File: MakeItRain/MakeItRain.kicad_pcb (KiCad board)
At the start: 4 copper layers, 151.1 x 71.1 mm, 80 parts, among them IC3 OPA2340PA, IC4 LTV-846S, J1 Conn_02x15_Odd_Even, J2 Conn_02x19_Odd_Even, J3 Conn_01x19, J4 Conn_01x01, J5 Conn_01x04, P1 Screw_Terminal_01x02, Q1 2N7000, Q10 2N7000, Q11 2N7000, Q12 IRF9Z34NPBF, Q13 IRF9Z34NPBF, Q2 2N7000, Q3 IRF9Z34NPBF, Q4 2N7000, Q5 2N7000, Q6 IRF9Z34NPBF, Q7 2N7000, Q8 2N7000, Q9 IRF9Z34NPBF, U2 178.6165.0001

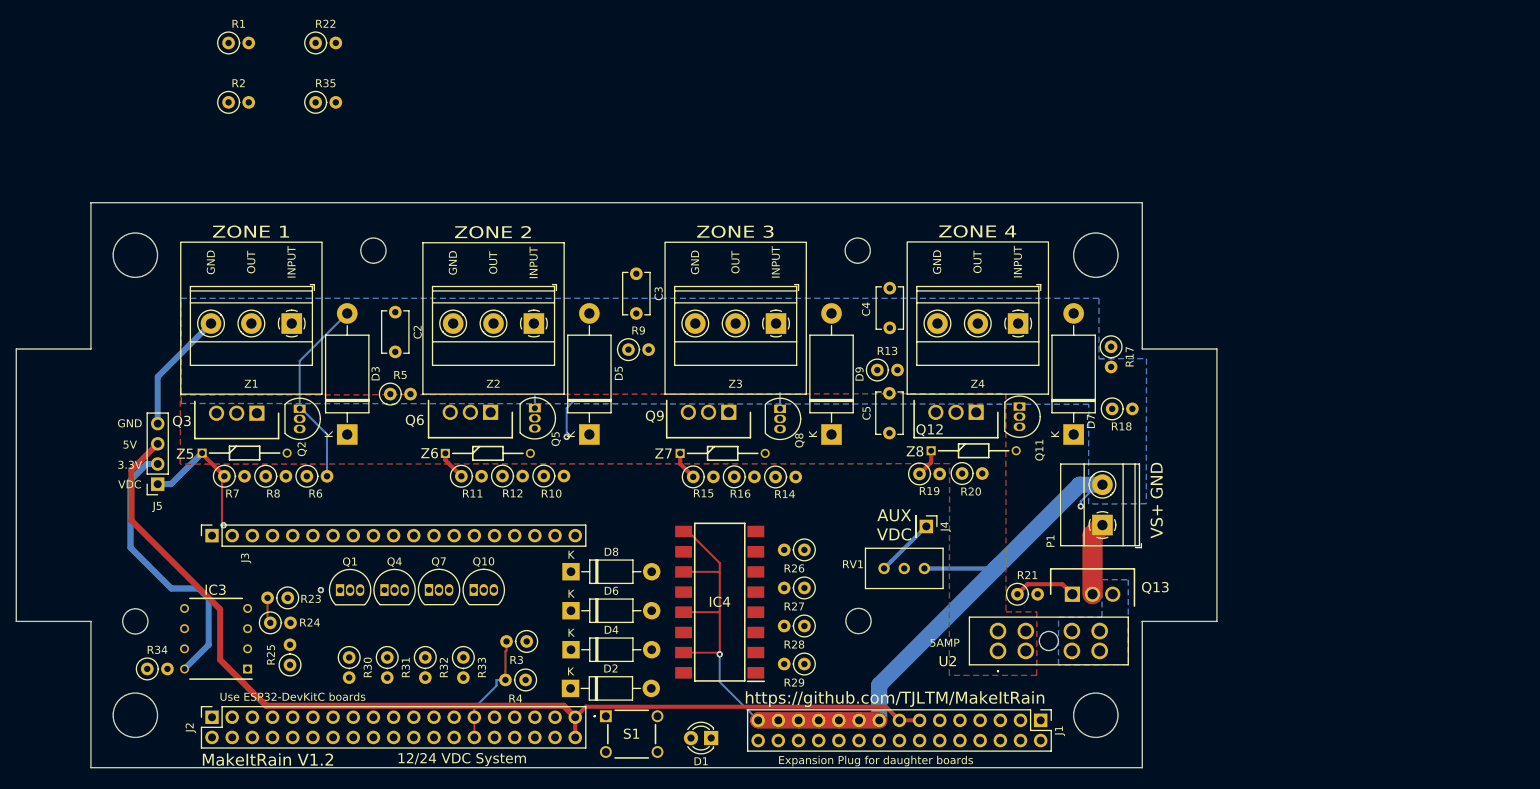
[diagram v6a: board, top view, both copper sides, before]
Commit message: working on getting the test code for the MCP23008 into the fw. working on the pins and getting all of that stuff placed on the PCB.
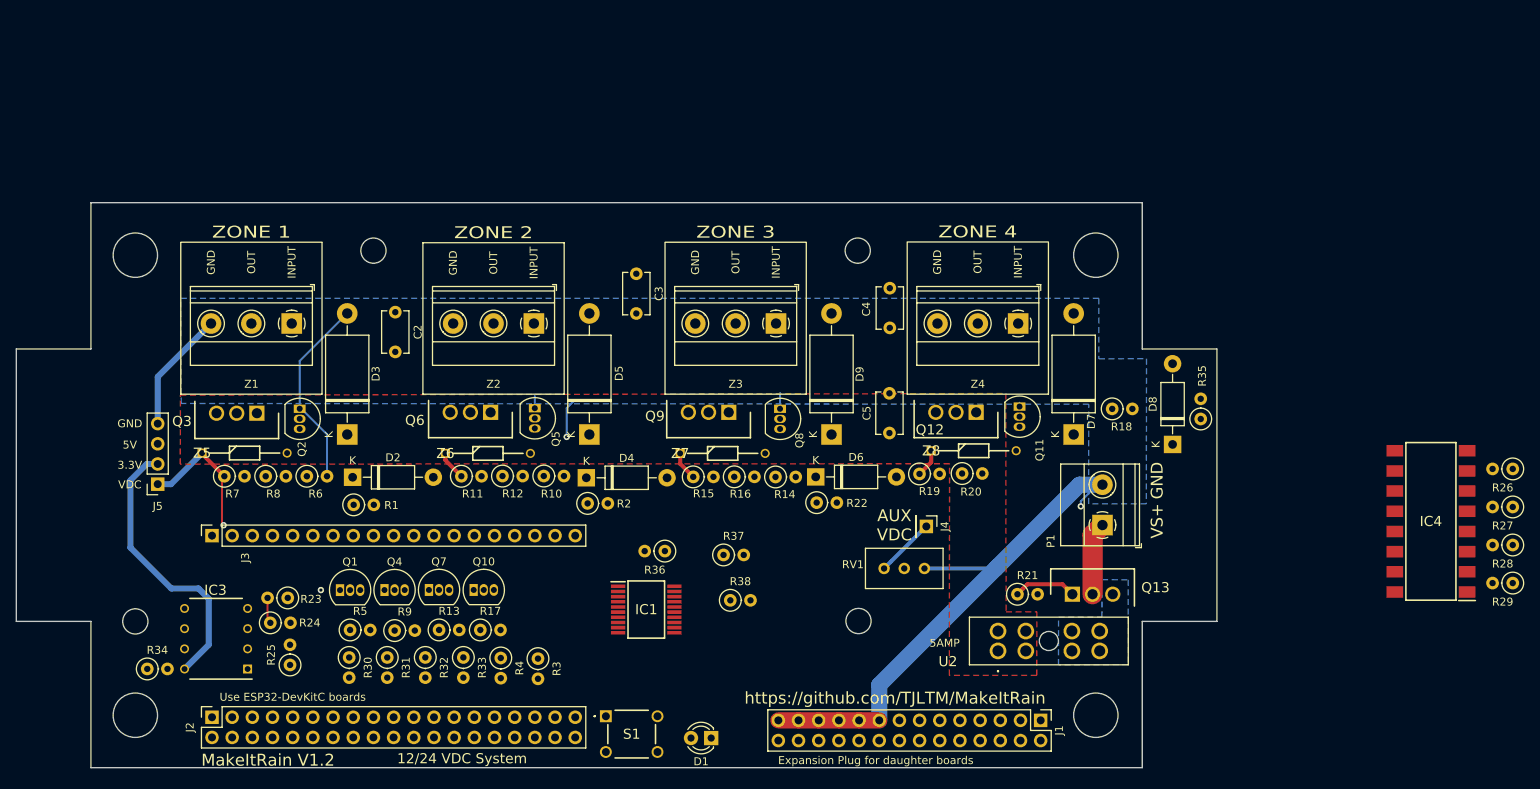
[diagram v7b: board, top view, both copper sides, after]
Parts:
- added IC1: MCP23008T-E_SS, SamacSys_Parts:SOP65P780X200-20N, F.Cu at (120.7, 107.1)
- added R36: 10k, Resistor_THT:R_Axial_DIN0207_L6.3mm_D2.5mm_P2.54mm_Vertical, F.Cu at (123.0, 99.7)
- added R37: 10k, Resistor_THT:R_Axial_DIN0207_L6.3mm_D2.5mm_P2.54mm_Vertical, F.Cu at (130.4, 100.2)
- added R38: 10k, Resistor_THT:R_Axial_DIN0207_L6.3mm_D2.5mm_P2.54mm_Vertical, F.Cu at (131.3, 105.9)
- J1: value Conn_02x15_Odd_Even -> Conn_02x14_Odd_Even; footprint Connector_PinHeader_2.54mm:PinHeader_2x15_P2.54mm_Vertical -> Connector_PinHeader_2.54mm:PinHeader_2x14_P2.54mm_Vertical
- moved R35 118.3 mm to (190.5, 83.1), turned to 90 degrees
- moved IC4 90.1 mm to (219.5, 96.0)
- moved R26 89.7 mm to (229.8, 89.4)
- moved R27 89.7 mm to (229.8, 94.2)
- moved R28 89.7 mm to (229.8, 99.0)
- moved R29 89.7 mm to (229.8, 103.8)
- moved R17 87.0 mm to (99.8, 109.7), turned to 0 degrees
- moved R22 85.6 mm to (142.2, 93.6)
- moved D8 77.4 mm to (187.0, 86.3), turned to 90 degrees
- moved R2 67.8 mm to (113.3, 93.7)
- moved R13 64.1 mm to (94.6, 109.7)
- moved R1 60.2 mm to (83.9, 93.9)
- moved R9 46.0 mm to (89.0, 109.7)
- moved D2 38.2 mm to (83.7, 90.4)
- moved D6 35.1 mm to (142.0, 90.4)
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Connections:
- net /Zone1IO/ZoneOutputTTL renamed Z1
- net /Zone2IO/ZoneOutputTTL renamed Z2
- net /Zone3IO/ZoneOutputTTL renamed Z3
- net /Zone4IO/ZoneOutputTTL renamed Z4
- IC3 pad 1: D36 -> D25
- IC3 pad 2: D36 -> D25
- J1 pad 10: unconnected-(J1-Pad10) -> Z6
- J1 pad 12: unconnected-(J1-Pad12) -> Z5
- J1 pad 13: +5V -> +3V3
- J1 pad 14: unconnected-(J1-Pad14) -> D26
- J1 pad 16: unconnected-(J1-Pad16) -> D23
- J1 pad 17: GND -> +5V
- J1 pad 18: unconnected-(J1-Pad18) -> D19
- J1 pad 19: GND -> +5V
- J1 pad 20: unconnected-(J1-Pad20) -> D18
- J1 pad 22: unconnected-(J1-Pad22) -> D17
- J1 pad 24: unconnected-(J1-Pad24) -> D16
- J1 pad 26: unconnected-(J1-Pad26) -> TX
- J1 pad 28: TX -> RX
- J1 pad 6: unconnected-(J1-Pad6) -> Z8
- J1 pad 8: unconnected-(J1-Pad8) -> Z7
- J1 pad 9: +VDC -> +3V3
- J2 pad 35: unconnected-(J2-Pad35) -> GND
- R25 pad 1: D36 -> D25
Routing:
- net +5V: track 128.0 -> 0.00 mm
- net +3V3: track 163.2 -> 35.4 mm
- net GND: track 296.1 -> 230.2 mm, vias 4 -> 3

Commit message: removed the 5V on the baseboard and daughterboard plug.
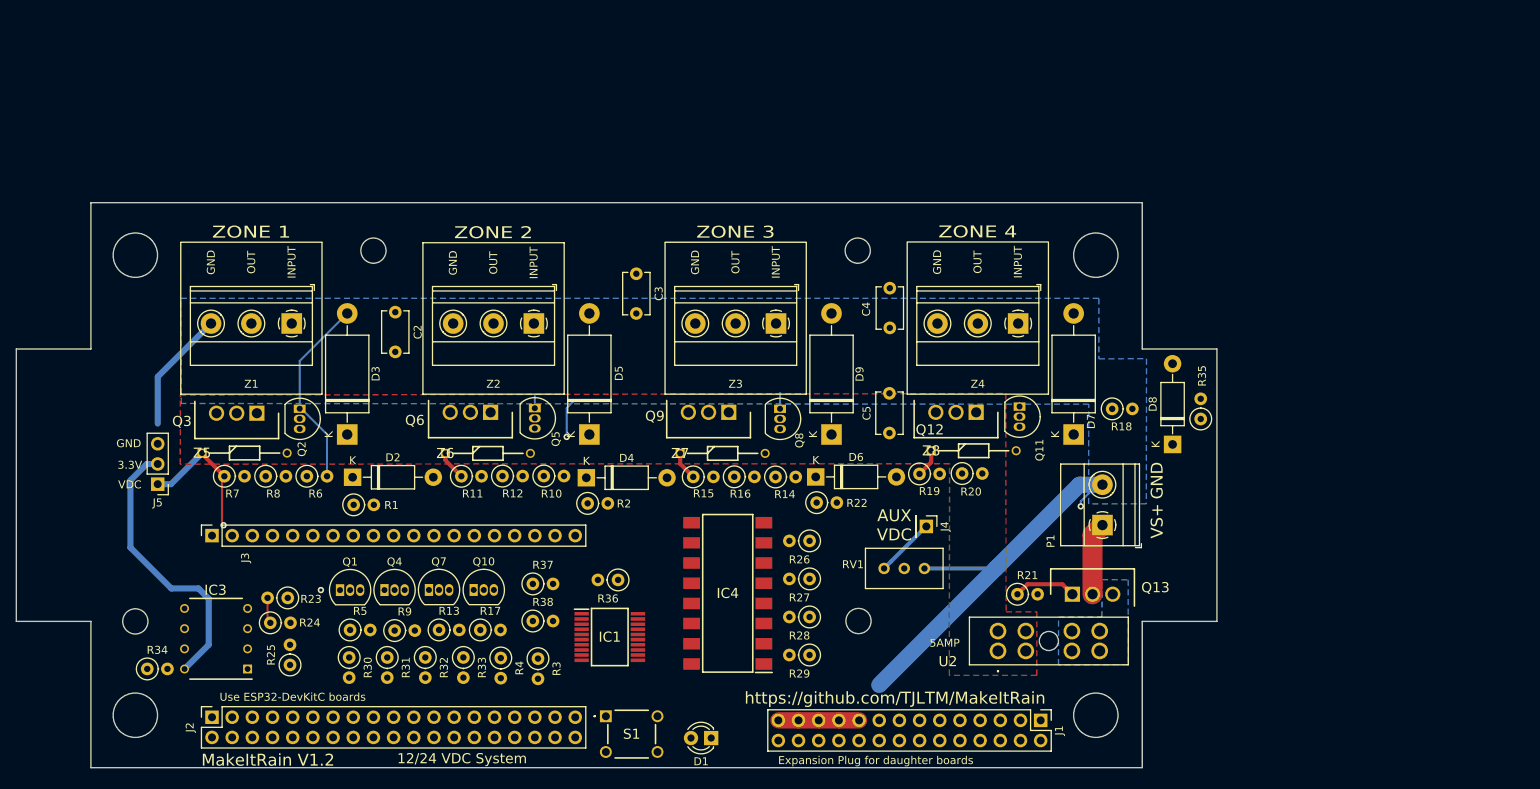
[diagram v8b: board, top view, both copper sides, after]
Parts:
- J5: value Conn_01x04 -> Conn_01x03; footprint Connector_PinSocket_2.54mm:PinSocket_1x04_P2.54mm_Vertical -> Connector_PinHeader_2.54mm:PinHeader_1x03_P2.54mm_Vertical
- moved IC4 89.0 mm to (131.0, 105.0)
- moved R26 89.0 mm to (141.3, 98.4)
- moved R27 89.0 mm to (141.3, 103.2)
- moved R28 89.0 mm to (141.3, 108.0)
- moved R29 89.0 mm to (141.3, 112.8)
- moved R38 25.0 mm to (106.4, 108.5)
- moved R37 24.3 mm to (106.4, 103.9)
- moved R36 6.92 mm to (117.2, 103.4)
- moved IC1 5.75 mm to (116.1, 110.6)
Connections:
- J1 pad 15: +5V -> +3V3
- J1 pad 17: +5V -> +3V3
- J1 pad 19: +5V -> GND
- J1 pad 9: +3V3 -> +VDC
- J2 pad 36: unconnected-(J2-Pad36) -> GND
- J2 pad 37: +5V -> Net-(J2-Pad37)
- J2 pad 38: +5V -> Net-(J2-Pad37)
- J5 pad 3: +5V -> GND
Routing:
- net GND: track 230.2 -> 223.2 mm
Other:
- board text removed: "5V"
